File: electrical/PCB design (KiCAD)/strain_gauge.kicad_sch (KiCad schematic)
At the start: 11 parts, among them U6 INA125U

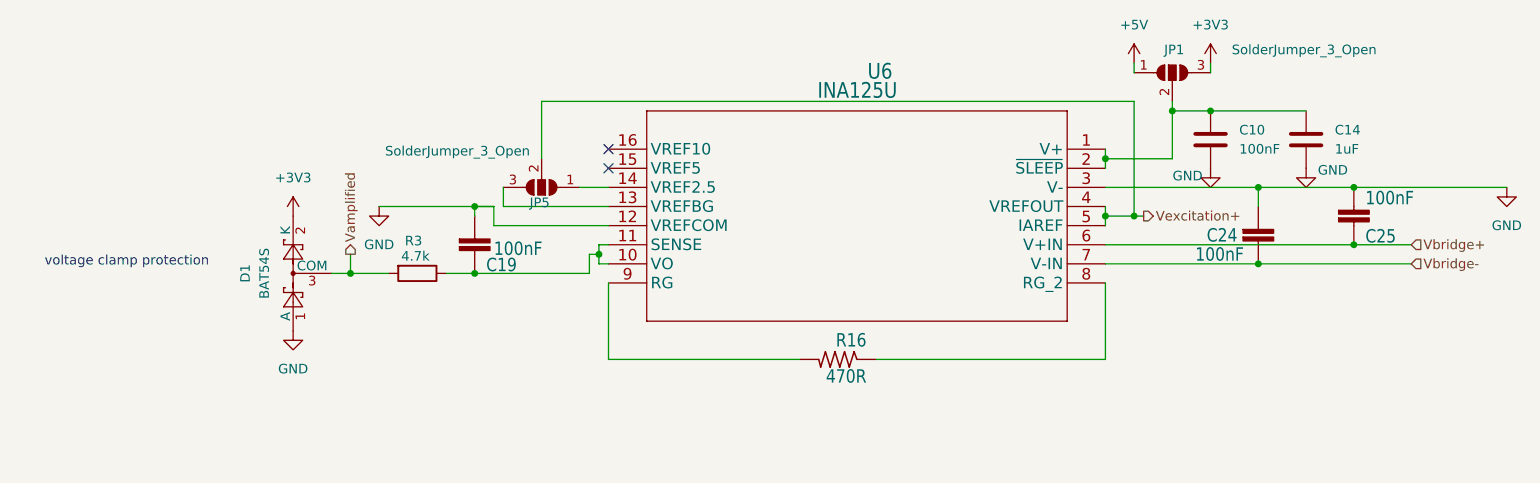
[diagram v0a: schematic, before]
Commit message: 26/06 schematics updates
see the changelog on the documentation /electrical/pcb
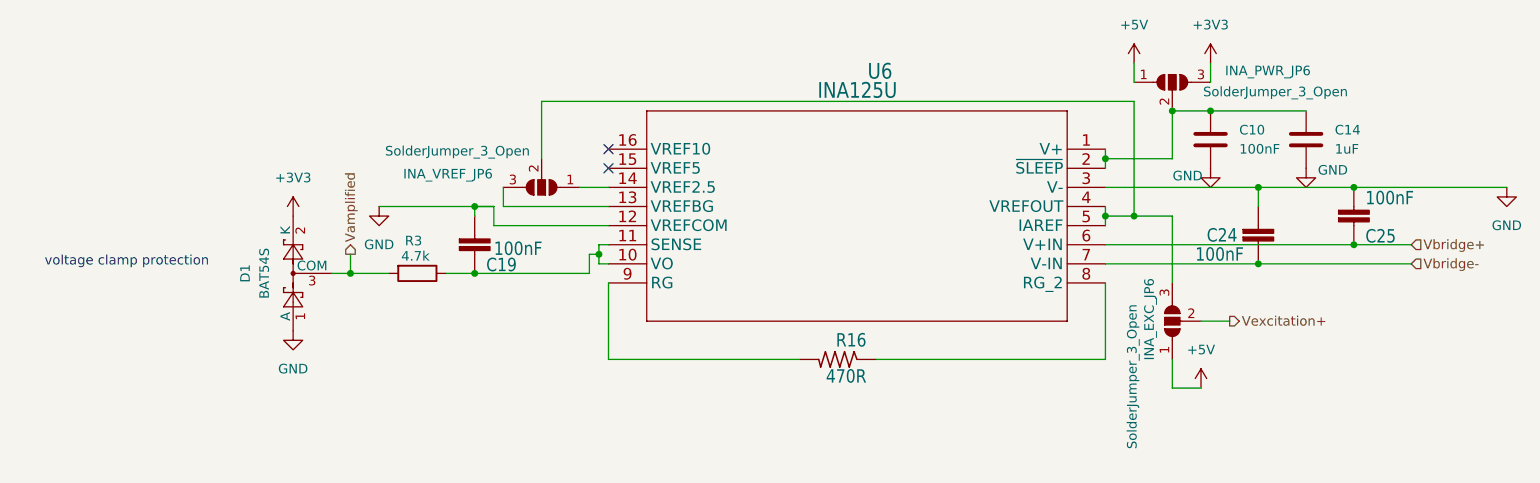
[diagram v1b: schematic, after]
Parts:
- added INA_EXC_JP6: SolderJumper_3_Open, Jumper:SolderJumper-3_P1.3mm_Open_RoundedPad1.0x1.5mm_NumberLabels, symbol Jumper:SolderJumper_3_Open
- renumbered JP1 to INA_PWR_JP6, JP5 to INA_VREF_JP6
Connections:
- net +5V: now also INA_EXC_JP6.1 (A)
- net Vexcitation+: now also INA_EXC_JP6.2 (C); no longer INA_VREF_JP6.2 (C), U6.4 (VREFOUT), U6.5 (IAREF)
- new net: INA_EXC_JP6.3 (B), INA_VREF_JP6.2 (C), U6.4 (VREFOUT), U6.5 (IAREF)
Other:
- moved on the sheet: INA_PWR_JP6
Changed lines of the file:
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@@
 	(wire
 		(pts
-			(xy 160.02 53.34) (xy 160.02 54.61)
+			(xy 165.1 92.71) (xy 165.1 96.52)
 		)
 		(stroke
@@
 	(wire
 		(pts
-			(xy 55.88 78.74) (xy 55.88 81.28)
+			(xy 160.02 53.34) (xy 160.02 55.88)
 		)
 		(stroke
@@
 	(wire
 		(pts
-			(xy 176.53 69.85) (xy 189.23 69.85)
+			(xy 55.88 78.74) (xy 55.88 81.28)
 		)
 		(stroke
@@
 	(wire
 		(pts
-			(xy 170.18 53.34) (xy 170.18 54.61)
+			(xy 176.53 69.85) (xy 189.23 69.85)
 		)
 		(stroke
@@
 	(wire
 		(pts
+			(xy 170.18 53.34) (xy 170.18 55.88)
+		)
+		(stroke
+			(width 0)
+			(type default)
+		)
+	)
+	(wire
+		(pts
 			(xy 74.93 74.93) (xy 90.17 74.93)
 		)
@@
 	(wire
 		(pts
-			(xy 88.9 80.01) (xy 90.17 80.01)
+			(xy 165.1 96.52) (xy 168.91 96.52)
 		)
 		(stroke
@@
 	(wire
 		(pts
-			(xy 160.02 58.42) (xy 160.02 73.66)
+			(xy 88.9 80.01) (xy 90.17 80.01)
 		)
 		(stroke
@@
 	(wire
 		(pts
+			(xy 160.02 58.42) (xy 160.02 73.66)
+		)
+		(stroke
+			(width 0)
+			(type default)
+		)
+	)
+	(wire
+		(pts
+			(xy 165.1 73.66) (xy 165.1 82.55)
+		)
+		(stroke
+			(width 0)
+			(type default)
+		)
+	)
+	(wire
+		(pts
 			(xy 156.21 77.47) (xy 189.23 77.47)
 		)
@@
 	(wire
 		(pts
-			(xy 160.02 73.66) (xy 161.29 73.66)
+			(xy 160.02 73.66) (xy 165.1 73.66)
 		)
 		(stroke
@@
 	(wire
 		(pts
-			(xy 72.39 72.39) (xy 74.93 72.39)
+			(xy 168.91 87.63) (xy 172.72 87.63)
 		)
 		(stroke
@@
 	(wire
 		(pts
+			(xy 72.39 72.39) (xy 74.93 72.39)
+		)
+		(stroke
+			(width 0)
+			(type default)
+		)
+	)
+	(wire
+		(pts
 			(xy 90.17 92.71) (xy 115.57 92.71)
 		)
@@
 	(wire
 		(pts
-			(xy 165.1 58.42) (xy 165.1 59.69)
+			(xy 156.21 80.01) (xy 176.53 80.01)
 		)
 		(stroke
@@
 	(wire
 		(pts
-			(xy 156.21 80.01) (xy 176.53 80.01)
+			(xy 176.53 72.39) (xy 176.53 69.85)
+		)
+		(stroke
+			(width 0.1524)
+			(type solid)
+		)
+	)
+	(wire
+		(pts
+			(xy 81.28 58.42) (xy 160.02 58.42)
 		)
 		(stroke
@@
 	(wire
 		(pts
-			(xy 176.53 72.39) (xy 176.53 69.85)
+			(xy 176.53 80.01) (xy 196.85 80.01)
 		)
 		(stroke
@@
 	(wire
 		(pts
-			(xy 81.28 58.42) (xy 160.02 58.42)
+			(xy 86.36 69.85) (xy 90.17 69.85)
 		)
 		(stroke
@@
 	(wire
 		(pts
-			(xy 176.53 80.01) (xy 196.85 80.01)
+			(xy 74.93 72.39) (xy 74.93 74.93)
 		)
 		(stroke
@@
 	(wire
 		(pts
-			(xy 86.36 69.85) (xy 90.17 69.85)
-		)
-		(stroke
-			(width 0)
-			(type default)
-		)
-	)
-	(wire
-		(pts
-			(xy 74.93 72.39) (xy 74.93 74.93)
+			(xy 72.39 81.28) (xy 87.63 81.28)
 		)
 		(stroke
@@
 		)
 	)
-	(wire
-		(pts
-			(xy 72.39 81.28) (xy 87.63 81.28)
-		)
-		(stroke
-			(width 0.1524)
-			(type solid)
-		)
-	)
 	(hierarchical_label "Vexcitation+"
 		(shape output)
-		(at 161.29 73.66 0)
+		(at 172.72 87.63 0)
 		(effects
 			(font
@@
 	)
 	(symbol
+		(lib_id "power:+5V")
+		(at 168.91 96.52 0)
+		(unit 1)
+		(exclude_from_sim no)
+		(in_bom yes)
+		(on_board yes)
+		(dnp no)
+		(fields_autoplaced yes)
+		(property "Reference" "#PWR085"
+			(at 168.91 100.33 0)
+			(effects
+				(font
+					(size 1.27 1.27)
+				)
+				(hide yes)
+			)
+		)
+		(property "Value" "+5V"
+			(at 168.91 91.44 0)
+			(effects
+				(font
+					(size 1.27 1.27)
+				)
+			)
+		)
+		(property "Footprint" ""
+			(at 168.91 96.52 0)
+			(effects
+				(font
+					(size 1.27 1.27)
+				)
+				(hide yes)
+			)
+		)
+		(property "Datasheet" ""
+			(at 168.91 96.52 0)
+			(effects
+				(font
+					(size 1.27 1.27)
+				)
+				(hide yes)
+			)
+		)
+		(property "Description" "Power symbol creates a global label with name \"+5V\""
+			(at 168.91 96.52 0)
+			(effects
+				(font
+					(size 1.27 1.27)
+				)
+				(hide yes)
+			)
+		)
+		(pin "1"
+		)
+		(instances
+			(project "TMotor_Rev0_5_1_Mark_2_NAU_OpenExo"
+				(path "/3e3ff72e-d777-45cf-9299-e91389ff12dd/76f1db6b-86f9-4936-9afd-1ff77552b608/4c7844ce-912f-4570-97a6-8e3b66425452"
+					(reference "#PWR088")
+					(unit 1)
+				)
+				(path "/3e3ff72e-d777-45cf-9299-e91389ff12dd/76f1db6b-86f9-4936-9afd-1ff77552b608/944478cc-ad75-4fe3-a0cb-a0388ad7c18d"
+					(reference "#PWR086")
+					(unit 1)
+				)
+				(path "/3e3ff72e-d777-45cf-9299-e91389ff12dd/76f1db6b-86f9-4936-9afd-1ff77552b608/c0c136a9-715a-4523-84cb-168ac7440c43"
+					(reference "#PWR087")
+					(unit 1)
+				)
+				(path "/3e3ff72e-d777-45cf-9299-e91389ff12dd/76f1db6b-86f9-4936-9afd-1ff77552b608/ffb5542d-bbdd-4da7-9ada-f3fec1753454"
+					(reference "#PWR085")
+					(unit 1)
+				)
+			)
+		)
+	)
+	(symbol
 		(lib_id "Device:C")
 		(at 182.88 63.5 0)
@@
 	)
 	(symbol
+		(lib_id "Jumper:SolderJumper_3_Open")
+		(at 165.1 87.63 90)
+		(unit 1)
+		(exclude_from_sim no)
+		(in_bom no)
+		(on_board yes)
+		(dnp no)
+		(property "Reference" "INA_EXC_JP6"
+			(at 162.052 87.376 0)
+			(effects
+				(font
+					(size 1.27 1.27)
+				)
+			)
+		)
+		(property "Value" "SolderJumper_3_Open"
+			(at 159.766 94.996 0)
+			(effects
+				(font
+					(size 1.27 1.27)
+				)
+			)
+		)
+		(property "Footprint" "Jumper:SolderJumper-3_P1.3mm_Open_RoundedPad1.0x1.5mm_NumberLabels"
+			(at 165.1 87.63 0)
+			(effects
+				(font
+					(size 1.27 1.27)
+				)
+				(hide yes)
+			)
+		)
+		(property "Datasheet" "~"
+			(at 165.1 87.63 0)
+			(effects
+				(font
+					(size 1.27 1.27)
+				)
+				(hide yes)
+			)
+		)
+		(property "Description" "Solder Jumper, 3-pole, open"
+			(at 165.1 87.63 0)
+			(effects
+				(font
+					(size 1.27 1.27)
+				)
+				(hide yes)
+			)
+		)
+		(pin "1"
+		)
+		(pin "2"
+		)
+		(pin "3"
+		)
+		(instances
+			(project "TMotor_Rev0_5_1_Mark_2_NAU_OpenExo"
+				(path "/3e3ff72e-d777-45cf-9299-e91389ff12dd/76f1db6b-86f9-4936-9afd-1ff77552b608/4c7844ce-912f-4570-97a6-8e3b66425452"
+					(reference "INA_EXC_JP7")
+					(unit 1)
+				)
+				(path "/3e3ff72e-d777-45cf-9299-e91389ff12dd/76f1db6b-86f9-4936-9afd-1ff77552b608/944478cc-ad75-4fe3-a0cb-a0388ad7c18d"
+					(reference "INA_EXC_JP3")
+					(unit 1)
+				)
+				(path "/3e3ff72e-d777-45cf-9299-e91389ff12dd/76f1db6b-86f9-4936-9afd-1ff77552b608/c0c136a9-715a-4523-84cb-168ac7440c43"
+					(reference "INA_EXC_JP4")
+					(unit 1)
+				)
+				(path "/3e3ff72e-d777-45cf-9299-e91389ff12dd/76f1db6b-86f9-4936-9afd-1ff77552b608/ffb5542d-bbdd-4da7-9ada-f3fec1753454"
+					(reference "INA_EXC_JP6")
+					(unit 1)
+				)
+			)
+		)
+	)
+	(symbol
 		(lib_id "Diode:BAT54S")
 		(at 48.26 81.28 90)
@@
 	(symbol
 		(lib_id "Jumper:SolderJumper_3_Open")
-		(at 165.1 54.61 0)
+		(at 165.1 55.88 0)
 		(unit 1)
 		(exclude_from_sim no)
@@
 		(on_board yes)
 		(dnp no)
-		(property "Reference" "JP1"
-			(at 165.354 51.562 0)
+		(property "Reference" "INA_PWR_JP6"
+			(at 177.8 54.356 0)
 			(effects
 				(font
@@
 		)
 		(property "Value" "SolderJumper_3_Open"
-			(at 182.626 51.562 0)
+			(at 178.816 57.15 0)
 			(effects
 				(font
@@
 		)
 		(property "Footprint" "Jumper:SolderJumper-3_P1.3mm_Open_RoundedPad1.0x1.5mm_NumberLabels"
-			(at 165.1 54.61 0)
+			(at 165.1 55.88 0)
 			(effects
 				(font
@@
 		)
 		(property "Datasheet" "~"
-			(at 165.1 54.61 0)
+			(at 165.1 55.88 0)
 			(effects
 				(font
@@
 		)
 		(property "Description" "Solder Jumper, 3-pole, open"
-			(at 165.1 54.61 0)
+			(at 165.1 55.88 0)
 			(effects
 				(font
@@
 			(project ""
 				(path "/3e3ff72e-d777-45cf-9299-e91389ff12dd/76f1db6b-86f9-4936-9afd-1ff77552b608/4c7844ce-912f-4570-97a6-8e3b66425452"
-					(reference "JP4")
-					(unit 1)
-				)
-				(path "/3e3ff72e-d777-45cf-9299-e91389ff12dd/76f1db6b-86f9-4936-9afd-1ff77552b608/944478cc-ad75-4fe3-a0cb-a0388ad7c18d"
-					(reference "JP2")
-					(unit 1)
-				)
-				(path "/3e3ff72e-d777-45cf-9299-e91389ff12dd/76f1db6b-86f9-4936-9afd-1ff77552b608/c0c136a9-715a-4523-84cb-168ac7440c43"
-					(reference "JP3")
-					(unit 1)
-				)
-				(path "/3e3ff72e-d777-45cf-9299-e91389ff12dd/76f1db6b-86f9-4936-9afd-1ff77552b608/ffb5542d-bbdd-4da7-9ada-f3fec1753454"
-					(reference "JP1")
+					(reference "INA_PWR_JP7")
+					(unit 1)
+				)
+				(path "/3e3ff72e-d777-45cf-9299-e91389ff12dd/76f1db6b-86f9-4936-9afd-1ff77552b608/944478cc-ad75-4fe3-a0cb-a0388ad7c18d"
+					(reference "INA_PWR_JP3")
+					(unit 1)
+				)
+				(path "/3e3ff72e-d777-45cf-9299-e91389ff12dd/76f1db6b-86f9-4936-9afd-1ff77552b608/c0c136a9-715a-4523-84cb-168ac7440c43"
+					(reference "INA_PWR_JP4")
+					(unit 1)
+				)
+				(path "/3e3ff72e-d777-45cf-9299-e91389ff12dd/76f1db6b-86f9-4936-9afd-1ff77552b608/ffb5542d-bbdd-4da7-9ada-f3fec1753454"
+					(reference "INA_PWR_JP6")
 					(unit 1)
 				)
@@
 		(on_board yes)
 		(dnp no)
-		(property "Reference" "JP5"
-			(at 81.026 71.882 0)
+		(property "Reference" "INA_VREF_JP6"
+			(at 68.834 68.072 0)
 			(effects
 				(font
@@
 			(project "TMotor_Rev0_5_1_Mark_2_NAU_OpenExo"
 				(path "/3e3ff72e-d777-45cf-9299-e91389ff12dd/76f1db6b-86f9-4936-9afd-1ff77552b608/4c7844ce-912f-4570-97a6-8e3b66425452"
-					(reference "JP10")
-					(unit 1)
-				)
-				(path "/3e3ff72e-d777-45cf-9299-e91389ff12dd/76f1db6b-86f9-4936-9afd-1ff77552b608/944478cc-ad75-4fe3-a0cb-a0388ad7c18d"
-					(reference "JP8")
-					(unit 1)
-				)
-				(path "/3e3ff72e-d777-45cf-9299-e91389ff12dd/76f1db6b-86f9-4936-9afd-1ff77552b608/c0c136a9-715a-4523-84cb-168ac7440c43"
-					(reference "JP9")
-					(unit 1)
-				)
-				(path "/3e3ff72e-d777-45cf-9299-e91389ff12dd/76f1db6b-86f9-4936-9afd-1ff77552b608/ffb5542d-bbdd-4da7-9ada-f3fec1753454"
-					(reference "JP5")
-					(unit 1)
-				)
+					(reference "INA_VREF_JP7")
+					(unit 1)
+				)
+				(path "/3e3ff72e-d777-45cf-9299-e91389ff12dd/76f1db6b-86f9-4936-9afd-1ff77552b608/944478cc-ad75-4fe3-a0cb-a0388ad7c18d"
+					(reference "INA_VREF_JP3")
+					(unit 1)
+				)
+				(path "/3e3ff72e-d777-45cf-9299-e91389ff12dd/76f1db6b-86f9-4936-9afd-1ff77552b608/c0c136a9-715a-4523-84cb-168ac7440c43"
+					(reference "INA_VREF_JP4")
+					(unit 1)
+				)
+				(path "/3e3ff72e-d777-45cf-9299-e91389ff12dd/76f1db6b-86f9-4936-9afd-1ff77552b608/ffb5542d-bbdd-4da7-9ada-f3fec1753454"
+					(reference "INA_VREF_JP6")
+					(unit 1)
+				)
